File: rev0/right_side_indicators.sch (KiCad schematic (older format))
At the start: 21 parts, among them IC1 ECP5-BGA256

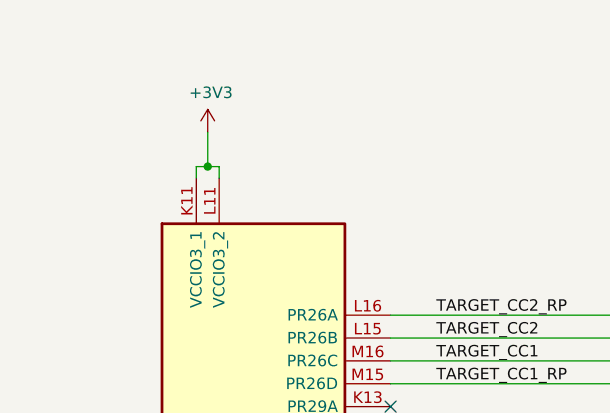
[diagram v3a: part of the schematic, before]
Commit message: hardware: add more test points
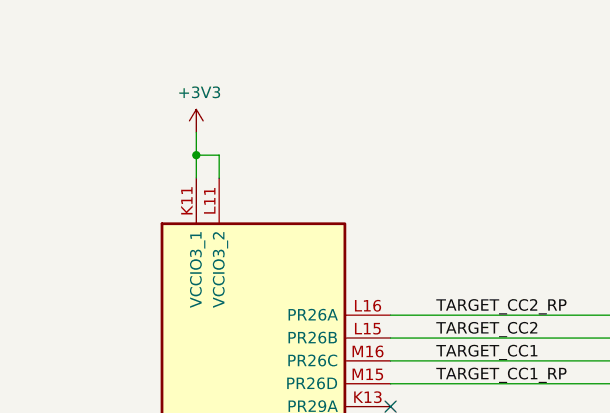
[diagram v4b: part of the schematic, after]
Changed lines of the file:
@@
 $Descr A4 11693 8268
 encoding utf-8
-Sheet 5 9
+Sheet 9 9
 Title "LUNA: Right Side I/O"
-Date "2021-01-04"
+Date "2021-01-05"
 Rev "r0"
 Comp "Copyright 2019-2021 Great Scott Gadgets"
@@
 $EndDescr
 Wire Wire Line
-	2150 1900 2150 1850
-Wire Wire Line
-	2150 1850 2200 1850
-Wire Wire Line
-	2250 1850 2250 1900
-Connection ~ 2200 1850
-Wire Wire Line
-	2200 1850 2250 1850
-Wire Wire Line
-	2200 1700 2200 1850
+	2150 1900 2150 1800
+Wire Wire Line
+	2250 1800 2250 1900
+Wire Wire Line
+	2150 1700 2150 1800
 $Comp
 L power:+3V3 #PWR086
 U 1 1 5DF1CB59
-P 2200 1700
-F 0 "#PWR086" H 2200 1550 50  0001 C CNN
-F 1 "+3V3" H 2214 1873 50  0000 C CNN
-F 2 "" H 2200 1700 50  0001 C CNN
-F 3 "" H 2200 1700 50  0001 C CNN
-	1    2200 1700
+P 2150 1700
+F 0 "#PWR086" H 2150 1550 50  0001 C CNN
+F 1 "+3V3" H 2164 1873 50  0000 C CNN
+F 2 "" H 2150 1700 50  0001 C CNN
+F 3 "" H 2150 1700 50  0001 C CNN
+	1    2150 1700
 	1    0    0    -1
 $EndComp
@@
 	0    1    -1   0
 $EndComp
+Connection ~ 2150 1800
+Wire Wire Line
+	2150 1800 2250 1800
 Wire Bus Line
 	5600 1200 5600 3700

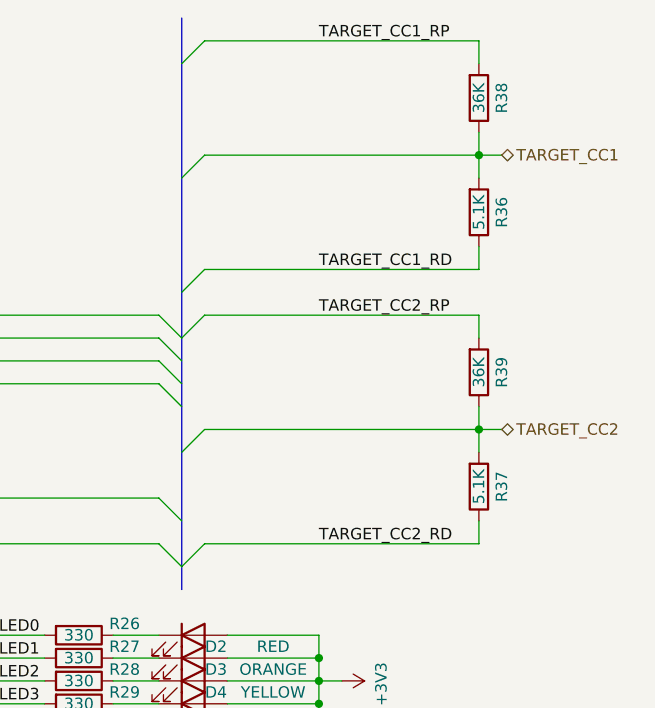
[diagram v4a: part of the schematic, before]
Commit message: hardware: clarify schematic
specify CC resistors as ±10% to hint that the spec requires it
add resistance value to resistor networks
give UART nets top-level names indicating JTAG functions
change AP22811 values to AP22811A
change PMOD to Pmod
nudge FPGA_TMS trace to make it more bodgeable
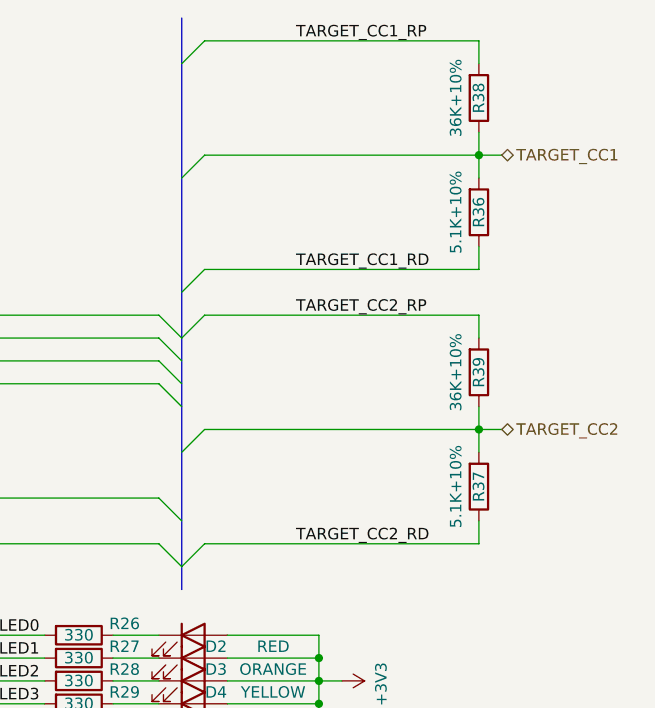
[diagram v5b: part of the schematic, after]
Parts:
- R36, R37: value 5.1K -> 5.1K+10%
- R38, R39: value 36K -> 36K+10%
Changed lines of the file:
@@
 Sheet 9 9
 Title "LUNA: Right Side I/O"
-Date "2021-01-05"
+Date "2021-01-08"
 Rev "r0"
 Comp "Copyright 2019-2021 Great Scott Gadgets"
@@
 AR Path="/60B354AE/61007651" Ref="R?"  Part="1"
 AR Path="/5DEF5588/61007651" Ref="R36"  Part="1"
-F 0 "R36" V 7000 2050 50  0000 C CNN
-F 1 "5.1K" V 6900 2050 50  0000 C CNN
+F 0 "R36" V 6900 2050 50  0000 C CNN
+F 1 "5.1K+10%" V 6800 2050 50  0000 C CNN
 F 2 "Resistor_SMD:R_0402_1005Metric" V 6830 2050 50  0001 C CNN
 F 3 "~" H 6900 2050 50  0001 C CNN
@@
 AR Path="/60B354AE/6100765E" Ref="R?"  Part="1"
 AR Path="/5DEF5588/6100765E" Ref="R37"  Part="1"
-F 0 "R37" V 7000 3250 50  0000 C CNN
-F 1 "5.1K" V 6900 3250 50  0000 C CNN
+F 0 "R37" V 6900 3250 50  0000 C CNN
+F 1 "5.1K+10%" V 6800 3250 50  0000 C CNN
 F 2 "Resistor_SMD:R_0402_1005Metric" V 6830 3250 50  0001 C CNN
 F 3 "~" H 6900 3250 50  0001 C CNN
@@
 AR Path="/60B354AE/6109E5AF" Ref="R?"  Part="1"
 AR Path="/5DEF5588/6109E5AF" Ref="R38"  Part="1"
-F 0 "R38" V 7000 1550 50  0000 C CNN
-F 1 "36K" V 6900 1550 50  0000 C CNN
+F 0 "R38" V 6900 1550 50  0000 C CNN
+F 1 "36K+10%" V 6800 1550 50  0000 C CNN
 F 2 "Resistor_SMD:R_0402_1005Metric" V 6830 1550 50  0001 C CNN
 F 3 "~" H 6900 1550 50  0001 C CNN
@@
 AR Path="/60B354AE/6112DB59" Ref="R?"  Part="1"
 AR Path="/5DEF5588/6112DB59" Ref="R39"  Part="1"
-F 0 "R39" V 7000 2750 50  0000 C CNN
-F 1 "36K" V 6900 2750 50  0000 C CNN
+F 0 "R39" V 6900 2750 50  0000 C CNN
+F 1 "36K+10%" V 6800 2750 50  0000 C CNN
 F 2 "Resistor_SMD:R_0402_1005Metric" V 6830 2750 50  0001 C CNN
 F 3 "~" H 6900 2750 50  0001 C CNN
@@
 Wire Wire Line
 	6900 3400 6900 3500
-Text Label 6200 2500 0    50   ~ 0
+Text Label 6100 2500 0    50   ~ 0
 TARGET_CC2_RP
-Text Label 6200 3500 0    50   ~ 0
+Text Label 6100 3500 0    50   ~ 0
 TARGET_CC2_RD
 Wire Wire Line
@@
 Wire Wire Line
 	4400 3400 3000 3400
-Text Label 6200 1300 0    50   ~ 0
+Text Label 6100 1300 0    50   ~ 0
 TARGET_CC1_RP
-Text Label 6200 2300 0    50   ~ 0
+Text Label 6100 2300 0    50   ~ 0
 TARGET_CC1_RD
 Wire Wire Line

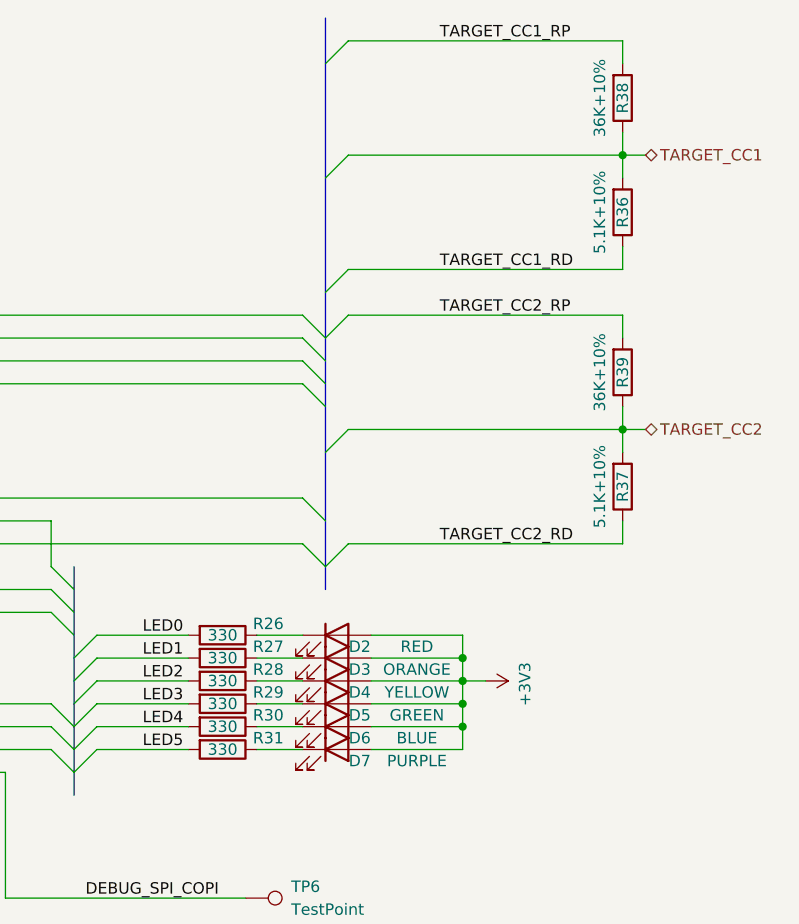
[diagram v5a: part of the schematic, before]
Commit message: hardware: select LEDs and series resistors
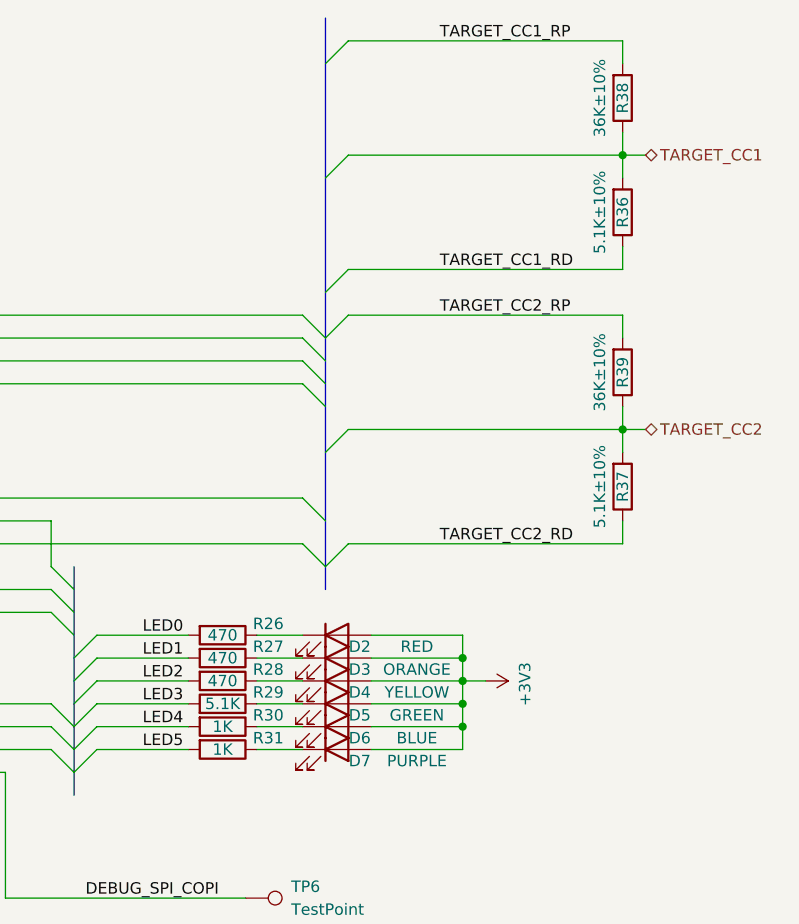
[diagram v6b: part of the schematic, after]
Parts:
- D2: Description (none) -> LED SMD 0603 RED; Manufacturer (none) -> OptoSupply; Part Number GENERIC-LED-0603-RED -> OSR50603C1E
- D3: Description (none) -> LED SMD 0603 ORANGE; Manufacturer (none) -> EKINGLUX; Part Number GENERIC-LED-0603-ORANGE -> E6C0603SEAC1UDA
- D4: Description (none) -> LED SMD 0603 YELLOW; Manufacturer (none) -> EKINGLUX; Part Number GENERIC-LED-0603-YELLOW -> E6C0603UYAC1UDA
- D5: Description (none) -> LED SMD 0603 GREEN; Manufacturer (none) -> Orient; Part Number GENERIC-LED-0603-GREEN -> ORH-G36G
- D6: Description (none) -> LED SMD 0603 BLUE; Manufacturer (none) -> Orient; Part Number GENERIC-LED-0603-BLUE -> ORH-B36G
- D7: Description (none) -> LED SMD 0603 VIOLET; Manufacturer (none) -> OptoSupply; Part Number GENERIC-LED-0603-PURPLE -> OSVX0603C1E
- R26, R27, R28: value 330 -> 470; Part Number GENERIC-RES-0402-330 -> GENERIC-RES-0402-470
- R29: value 330 -> 5.1K; Part Number GENERIC-RES-0402-330 -> GENERIC-RES-0402-5.1K
- R30, R31: value 330 -> 1K; Part Number GENERIC-RES-0402-330 -> GENERIC-RES-0402-1K
- R36, R37: value 5.1K+10% -> 5.1K±10%
- R38, R39: value 36K+10% -> 36K±10%
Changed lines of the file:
@@
 Sheet 9 9
 Title "LUNA: Right Side I/O"
-Date "2021-01-08"
+Date "2021-01-10"
 Rev "r0"
 Comp "Copyright 2019-2021 Great Scott Gadgets"
@@
 AR Path="/5DEF5588/61007651" Ref="R36"  Part="1"
 F 0 "R36" V 6900 2050 50  0000 C CNN
-F 1 "5.1K+10%" V 6800 2050 50  0000 C CNN
+F 1 "5.1K±10%" V 6800 2050 50  0000 C CNN
 F 2 "Resistor_SMD:R_0402_1005Metric" V 6830 2050 50  0001 C CNN
 F 3 "~" H 6900 2050 50  0001 C CNN
@@
 AR Path="/5DEF5588/6100765E" Ref="R37"  Part="1"
 F 0 "R37" V 6900 3250 50  0000 C CNN
-F 1 "5.1K+10%" V 6800 3250 50  0000 C CNN
+F 1 "5.1K±10%" V 6800 3250 50  0000 C CNN
 F 2 "Resistor_SMD:R_0402_1005Metric" V 6830 3250 50  0001 C CNN
 F 3 "~" H 6900 3250 50  0001 C CNN
@@
 AR Path="/5DEF5588/6109E5AF" Ref="R38"  Part="1"
 F 0 "R38" V 6900 1550 50  0000 C CNN
-F 1 "36K+10%" V 6800 1550 50  0000 C CNN
+F 1 "36K±10%" V 6800 1550 50  0000 C CNN
 F 2 "Resistor_SMD:R_0402_1005Metric" V 6830 1550 50  0001 C CNN
 F 3 "~" H 6900 1550 50  0001 C CNN
@@
 AR Path="/5DEF5588/6112DB59" Ref="R39"  Part="1"
 F 0 "R39" V 6900 2750 50  0000 C CNN
-F 1 "36K+10%" V 6800 2750 50  0000 C CNN
+F 1 "36K±10%" V 6800 2750 50  0000 C CNN
 F 2 "Resistor_SMD:R_0402_1005Metric" V 6830 2750 50  0001 C CNN
 F 3 "~" H 6900 2750 50  0001 C CNN
@@
 AR Path="/5DEF5588/61428AB0" Ref="R26"  Part="1"
 F 0 "R26" V 5100 4100 50  0000 C CNN
-F 1 "330" V 5150 3900 50  0000 C CNN
+F 1 "470" V 5150 3900 50  0000 C CNN
 F 2 "Resistor_SMD:R_0402_1005Metric" V 5080 3900 50  0001 C CNN
 F 3 "~" H 5150 3900 50  0001 C CNN
-F 4 "GENERIC-RES-0402-330" H 5150 3900 50  0001 C CNN "Part Number"
+F 4 "GENERIC-RES-0402-470" H 5150 3900 50  0001 C CNN "Part Number"
 F 5 "any equivalent" H 5150 3900 50  0001 C CNN "Substitution"
 	1    5150 3900
@@
 AR Path="/5DEF5588/61428AB7" Ref="R27"  Part="1"
 F 0 "R27" V 5100 4200 50  0000 C CNN
-F 1 "330" V 5150 4000 50  0000 C CNN
+F 1 "470" V 5150 4000 50  0000 C CNN
 F 2 "Resistor_SMD:R_0402_1005Metric" V 5080 4000 50  0001 C CNN
 F 3 "~" H 5150 4000 50  0001 C CNN
-F 4 "GENERIC-RES-0402-330" H 5150 4000 50  0001 C CNN "Part Number"
+F 4 "GENERIC-RES-0402-470" H 5150 4000 50  0001 C CNN "Part Number"
 F 5 "any equivalent" H 5150 4000 50  0001 C CNN "Substitution"
 	1    5150 4000
@@
 AR Path="/5DEF5588/61428ABE" Ref="R28"  Part="1"
 F 0 "R28" V 5100 4300 50  0000 C CNN
-F 1 "330" V 5150 4100 50  0000 C CNN
+F 1 "470" V 5150 4100 50  0000 C CNN
 F 2 "Resistor_SMD:R_0402_1005Metric" V 5080 4100 50  0001 C CNN
 F 3 "~" H 5150 4100 50  0001 C CNN
-F 4 "GENERIC-RES-0402-330" H 5150 4100 50  0001 C CNN "Part Number"
+F 4 "GENERIC-RES-0402-470" H 5150 4100 50  0001 C CNN "Part Number"
 F 5 "any equivalent" H 5150 4100 50  0001 C CNN "Substitution"
 	1    5150 4100
-	0    1    1    0
-$EndComp
-$Comp
-L Device:R R?
-U 1 1 61428AC5
-P 5150 4200
-AR Path="/61428AC5" Ref="R?"  Part="1"
-AR Path="/5DEF5588/61428AC5" Ref="R29"  Part="1"
-F 0 "R29" V 5100 4400 50  0000 C CNN
-F 1 "330" V 5150 4200 50  0000 C CNN
-F 2 "Resistor_SMD:R_0402_1005Metric" V 5080 4200 50  0001 C CNN
-F 3 "~" H 5150 4200 50  0001 C CNN
-F 4 "GENERIC-RES-0402-330" H 5150 4200 50  0001 C CNN "Part Number"
-F 5 "any equivalent" H 5150 4200 50  0001 C CNN "Substitution"
-	1    5150 4200
-	0    1    1    0
-$EndComp
-$Comp
-L Device:R R?
-U 1 1 61428ACC
-P 5150 4300
-AR Path="/61428ACC" Ref="R?"  Part="1"
-AR Path="/5DEF5588/61428ACC" Ref="R30"  Part="1"
-F 0 "R30" V 5100 4500 50  0000 C CNN
-F 1 "330" V 5150 4300 50  0000 C CNN
-F 2 "Resistor_SMD:R_0402_1005Metric" V 5080 4300 50  0001 C CNN
-F 3 "~" H 5150 4300 50  0001 C CNN
-F 4 "GENERIC-RES-0402-330" H 5150 4300 50  0001 C CNN "Part Number"
-F 5 "any equivalent" H 5150 4300 50  0001 C CNN "Substitution"
-	1    5150 4300
-	0    1    1    0
-$EndComp
-$Comp
-L Device:R R?
-U 1 1 61428AD3
-P 5150 4400
-AR Path="/61428AD3" Ref="R?"  Part="1"
-AR Path="/5DEF5588/61428AD3" Ref="R31"  Part="1"
-F 0 "R31" V 5100 4600 50  0000 C CNN
-F 1 "330" V 5150 4400 50  0000 C CNN
-F 2 "Resistor_SMD:R_0402_1005Metric" V 5080 4400 50  0001 C CNN
-F 3 "~" H 5150 4400 50  0001 C CNN
-F 4 "GENERIC-RES-0402-330" H 5150 4400 50  0001 C CNN "Part Number"
-F 5 "any equivalent" H 5150 4400 50  0001 C CNN "Substitution"
-	1    5150 4400
 	0    1    1    0
 $EndComp
@@
 F 2 "LED_SMD:LED_0603_1608Metric_Pad1.05x0.95mm_HandSolder" H 5650 3900 50  0001 C CNN
 F 3 "~" H 5650 3900 50  0001 C CNN
-F 4 "GENERIC-LED-0603-RED" H 5650 3900 50  0001 C CNN "Part Number"
+F 4 "OSR50603C1E" H 5650 3900 50  0001 C CNN "Part Number"
+F 5 "OptoSupply" H 5650 3900 50  0001 C CNN "Manufacturer"
+F 6 "LED SMD 0603 RED" H 5650 3900 50  0001 C CNN "Description"
 	1    5650 3900
 	1    0    0    -1
@@
 F 2 "LED_SMD:LED_0603_1608Metric_Pad1.05x0.95mm_HandSolder" H 5650 4100 50  0001 C CNN
 F 3 "~" H 5650 4100 50  0001 C CNN
-F 4 "GENERIC-LED-0603-YELLOW" H 5650 4100 50  0001 C CNN "Part Number"
+F 4 "E6C0603UYAC1UDA" H 5650 4100 50  0001 C CNN "Part Number"
+F 5 "EKINGLUX" H 5650 4100 50  0001 C CNN "Manufacturer"
+F 6 "LED SMD 0603 YELLOW" H 5650 4100 50  0001 C CNN "Description"
 	1    5650 4100
 	1    0    0    -1
@@
 F 2 "LED_SMD:LED_0603_1608Metric_Pad1.05x0.95mm_HandSolder" H 5650 4200 50  0001 C CNN
 F 3 "~" H 5650 4200 50  0001 C CNN
-F 4 "GENERIC-LED-0603-GREEN" H 5650 4200 50  0001 C CNN "Part Number"
+F 4 "ORH-G36G" H 5650 4200 50  0001 C CNN "Part Number"
+F 5 "Orient" H 5650 4200 50  0001 C CNN "Manufacturer"
+F 6 "LED SMD 0603 GREEN" H 5650 4200 50  0001 C CNN "Description"
 	1    5650 4200
 	1    0    0    -1
@@
 F 2 "LED_SMD:LED_0603_1608Metric_Pad1.05x0.95mm_HandSolder" H 5650 4300 50  0001 C CNN
 F 3 "~" H 5650 4300 50  0001 C CNN
-F 4 "GENERIC-LED-0603-BLUE" H 5650 4300 50  0001 C CNN "Part Number"
+F 4 "ORH-B36G" H 5650 4300 50  0001 C CNN "Part Number"
+F 5 "Orient" H 5650 4300 50  0001 C CNN "Manufacturer"
+F 6 "LED SMD 0603 BLUE" H 5650 4300 50  0001 C CNN "Description"
 	1    5650 4300
 	1    0    0    -1
@@
 F 2 "LED_SMD:LED_0603_1608Metric_Pad1.05x0.95mm_HandSolder" H 5650 4400 50  0001 C CNN
 F 3 "~" H 5650 4400 50  0001 C CNN
-F 4 "GENERIC-LED-0603-PURPLE" H 5650 4400 50  0001 C CNN "Part Number"
+F 4 "OSVX0603C1E" H 5650 4400 50  0001 C CNN "Part Number"
+F 5 "OptoSupply" H 5650 4400 50  0001 C CNN "Manufacturer"
+F 6 "LED SMD 0603 VIOLET" H 5650 4400 50  0001 C CNN "Description"
 	1    5650 4400
 	1    0    0    -1
@@
 F 2 "LED_SMD:LED_0603_1608Metric_Pad1.05x0.95mm_HandSolder" H 5650 4000 50  0001 C CNN
 F 3 "~" H 5650 4000 50  0001 C CNN
-F 4 "GENERIC-LED-0603-ORANGE" H 5650 4000 50  0001 C CNN "Part Number"
+F 4 "E6C0603SEAC1UDA" H 5650 4000 50  0001 C CNN "Part Number"
+F 5 "EKINGLUX" H 5650 4000 50  0001 C CNN "Manufacturer"
+F 6 "LED SMD 0603 ORANGE" H 5650 4000 50  0001 C CNN "Description"
 	1    5650 4000
 	1    0    0    -1
@@
 Wire Wire Line
 	2150 1800 2250 1800
+$Comp
+L Device:R R?
+U 1 1 5FFC7230
+P 5150 4200
+AR Path="/5FFC7230" Ref="R?"  Part="1"
+AR Path="/5DD754D4/5FFC7230" Ref="R?"  Part="1"
+AR Path="/5DCD9772/5FFC7230" Ref="R?"  Part="1"
+AR Path="/5DDDB747/5FFC7230" Ref="R?"  Part="1"
+AR Path="/60B354AE/5FFC7230" Ref="R?"  Part="1"
+AR Path="/5DEF5588/5FFC7230" Ref="R29"  Part="1"
+F 0 "R29" V 5200 4400 50  0000 C CNN
+F 1 "5.1K" V 5150 4200 50  0000 C CNN
+F 2 "Resistor_SMD:R_0402_1005Metric" V 5080 4200 50  0001 C CNN
+F 3 "~" H 5150 4200 50  0001 C CNN
+F 4 "GENERIC-RES-0402-5.1K" H 5150 4200 50  0001 C CNN "Part Number"
+F 5 "any equivalent" H 5150 4200 50  0001 C CNN "Substitution"
+	1    5150 4200
+	0    1    -1   0
+$EndComp
+$Comp
+L Device:R R?
+U 1 1 5FFD563E
+P 5150 4300
+AR Path="/5DCD9772/5FFD563E" Ref="R?"  Part="1"
+AR Path="/5DEF5588/5FFD563E" Ref="R30"  Part="1"
+F 0 "R30" V 5100 4500 50  0000 C CNN
+F 1 "1K" V 5150 4300 50  0000 C CNN
+F 2 "Resistor_SMD:R_0402_1005Metric" V 5080 4300 50  0001 C CNN
+F 3 "~" H 5150 4300 50  0001 C CNN
+F 4 "GENERIC-RES-0402-1K" H 5150 4300 50  0001 C CNN "Part Number"
+F 5 "any equivalent" H 5150 4300 50  0001 C CNN "Substitution"
+	1    5150 4300
+	0    1    1    0
+$EndComp
 Wire Bus Line
 	5600 1200 5600 3700
 Wire Bus Line
 	4500 3600 4500 4600
+$Comp
+L Device:R R?
+U 1 1 5FFD756F
+P 5150 4400
+AR Path="/5DCD9772/5FFD756F" Ref="R?"  Part="1"
+AR Path="/5DEF5588/5FFD756F" Ref="R31"  Part="1"
+F 0 "R31" V 5100 4600 50  0000 C CNN
+F 1 "1K" V 5150 4400 50  0000 C CNN
+F 2 "Resistor_SMD:R_0402_1005Metric" V 5080 4400 50  0001 C CNN
+F 3 "~" H 5150 4400 50  0001 C CNN
+F 4 "GENERIC-RES-0402-1K" H 5150 4400 50  0001 C CNN "Part Number"
+F 5 "any equivalent" H 5150 4400 50  0001 C CNN "Substitution"
+	1    5150 4400
+	0    1    1    0
+$EndComp
 $EndSCHEMATC
